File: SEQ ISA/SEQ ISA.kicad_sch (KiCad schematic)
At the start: 32 parts, among them IC1 TLX9310_TPL,F, J1 Conn_01x04_Pin, J2 Conn_01x01_Pin, J3 Conn_01x04_Pin, Q1 BS170F, SW1 PRISE JACK, SW2 SW_SPDT, U1 STM32L010C6T6R, U2 LD3985M33R_SOT23

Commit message: Seq review
added security button for launch detection, PWM motor and changd the regulator for a simpler one
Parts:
- removed C12: 100n, symbol Device:C
- removed U2: LD3985M33R_SOT23, Package_TO_SOT_SMD:SOT-23-5, symbol Regulator_Linear:LD3985M33R_SOT23
- added C7: 100n, symbol Device:C
- added M1: TOWERPRO SG90, symbol Motor:Motor_Servo
- added R6: 5.6k, symbol Device:R
- added SW3: INTERPTEUR, symbol Switch:SW_SPST
- added U3: LD1117S33TR_SOT223, Package_TO_SOT_SMD:SOT-223-3_TabPin2, symbol Regulator_Linear:LD1117S33TR_SOT223
- C13, C9: value 10n -> 100n
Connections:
- net GPIO_B5 is gone; now on net LAUNCH_STR: U1.41 (PB5)
- net +3.3V: now also SW3.1 (A), U3.2 (VO)
- net +5V: now also M1.2 (+)
- net GND: now also C7.2, M1.3 (-), U3.1 (GND)
- net VBAT: now also U3.3 (VI)
- net LAUNCH_STR: now reaches C9.1
- net LAUNCH_STR: now also C7.1, R6.2
- net GPIO_B4 renamed PWN_MOTOR
- net PWN_MOTOR: now also M1.1 (PWM)
- new net: R6.1, SW3.2 (B)
- no-connect marks 30 -> 28
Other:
- note added: "Boutton de sécurité"
- note added: "L'alimentation doit être différente de celle du séquenceur !"
- note added: "Ouverture de la trappe à parachute"
- note added: "Pensez à découpler le signale transmis: C:1Op"
- moved on the sheet: C13, C15, J3

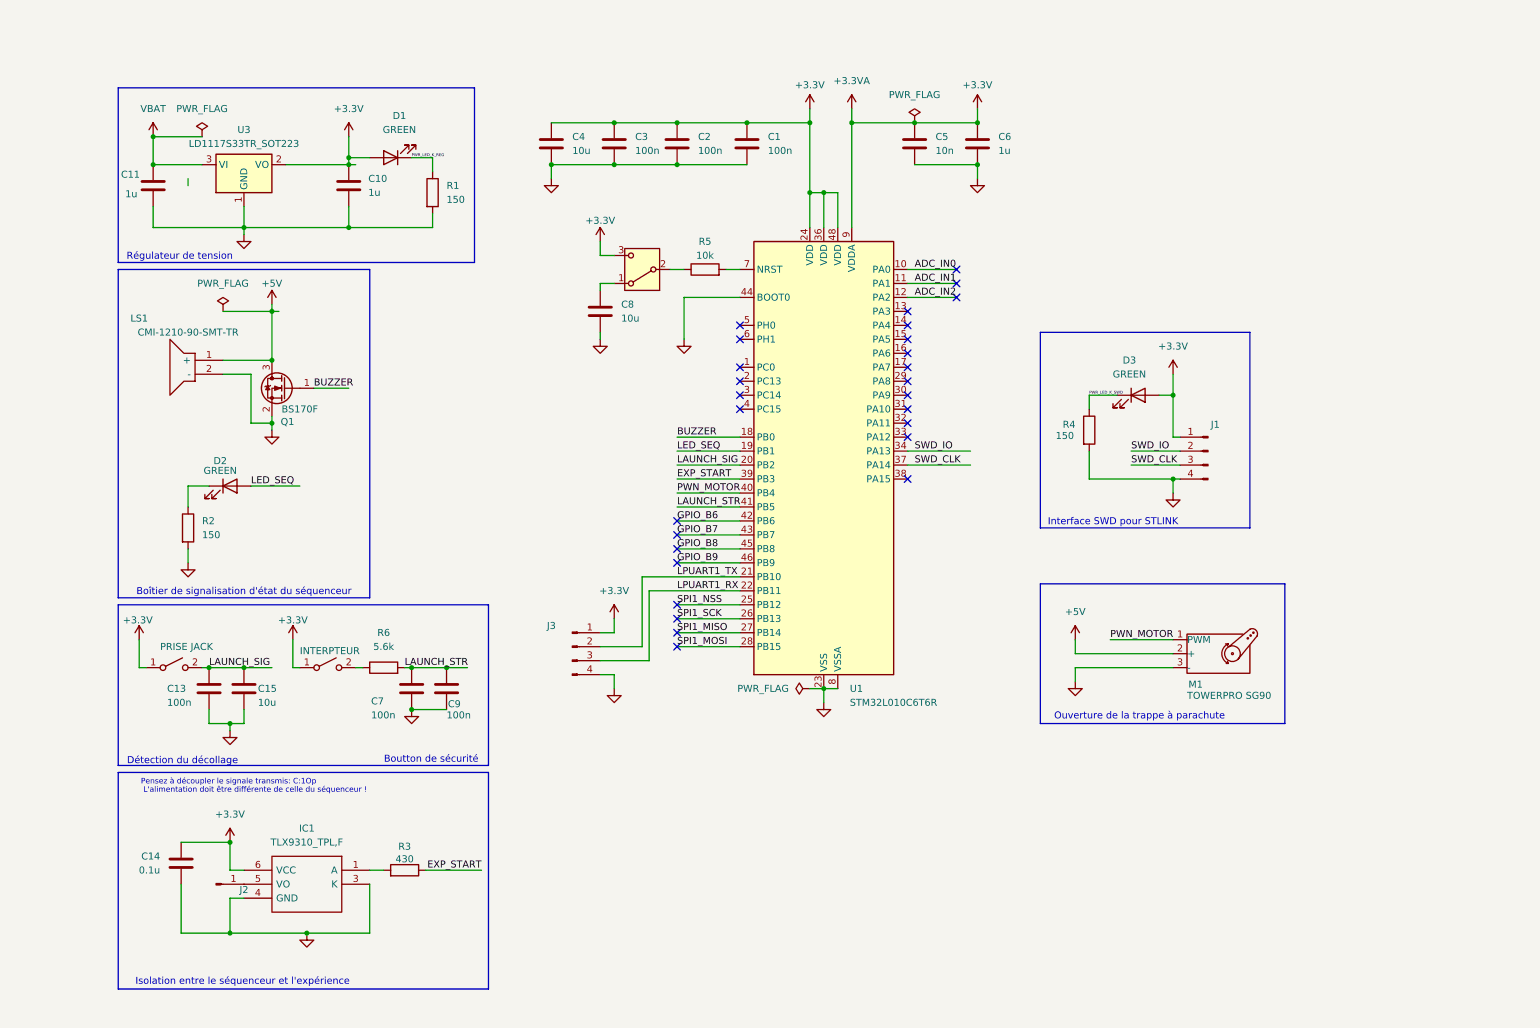
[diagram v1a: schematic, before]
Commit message: SEQ V2
Added servo motor controls, trigger button security for noise sensitive input and UART com
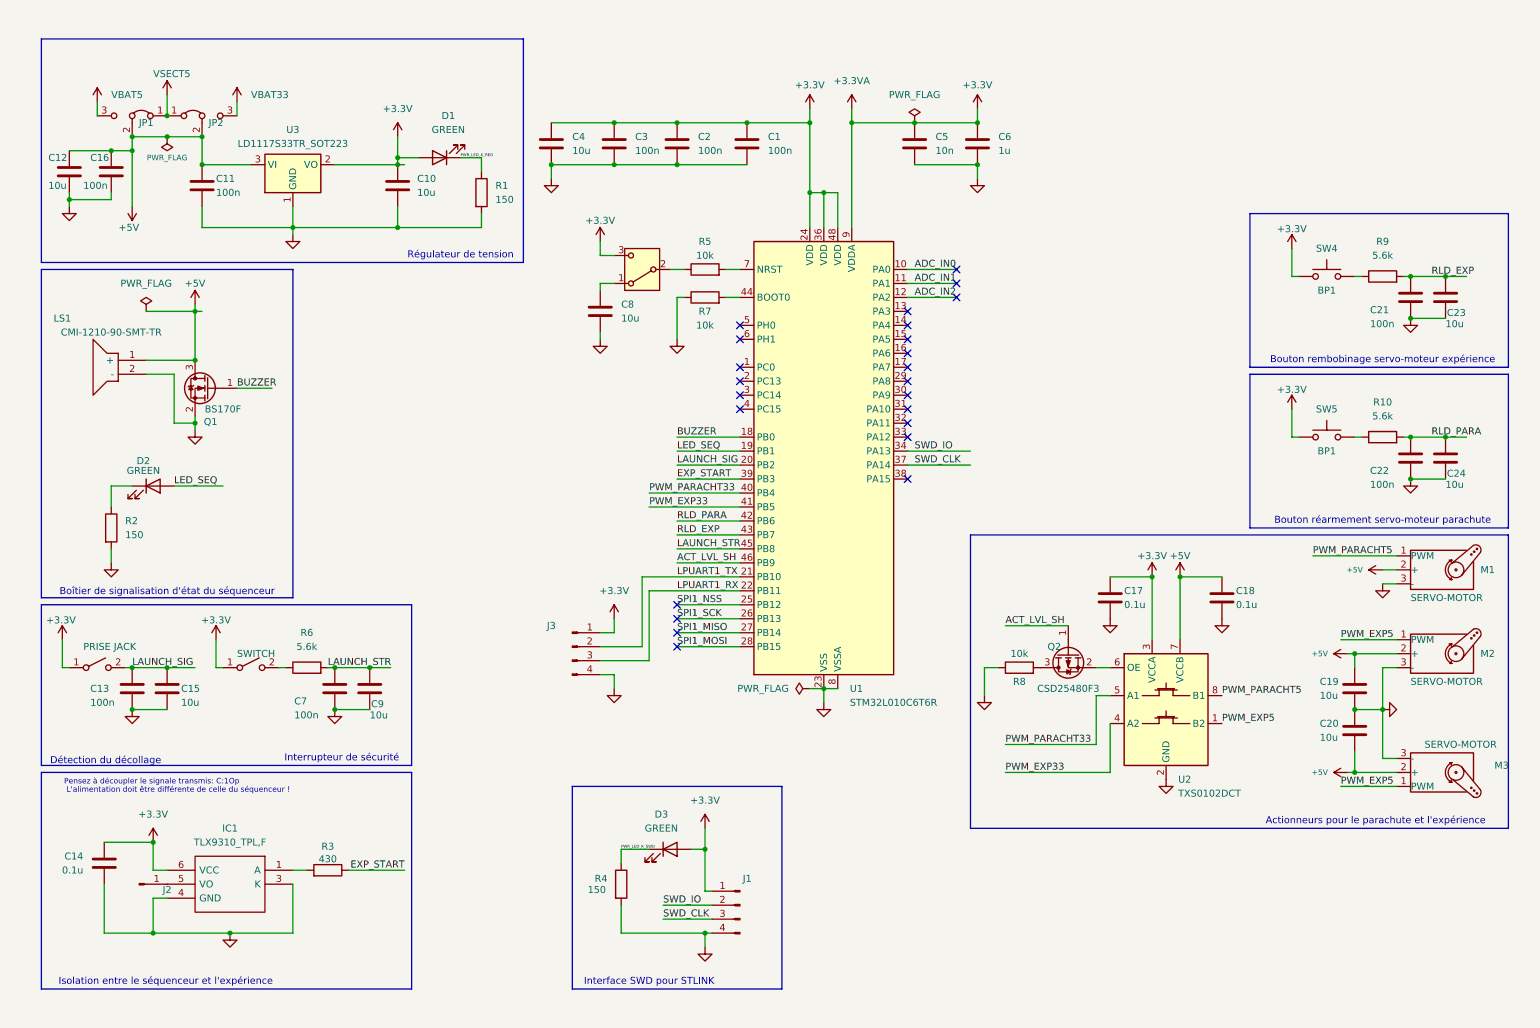
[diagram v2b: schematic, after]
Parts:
- added C12, C19, C20, C23, C24: 10u, symbol Device:C
- added C16, C21, C22: 100n, symbol Device:C
- added C17, C18: 0.1u, symbol Device:C
- added JP1, JP2: Jumper_3_Bridged12, symbol Jumper:Jumper_3_Bridged12
- added M2, M3: SERVO-MOTOR, symbol Motor:Motor_Servo
- added Q2: CSD25480F3, Package_DFN_QFN:Texas_PicoStar_DFN-3_0.69x0.60mm, symbol Transistor_FET:CSD25480F3
- added R10, R9: 5.6k, symbol Device:R
- added R7, R8: 10k, symbol Device:R
- added SW4, SW5: BP1, symbol Switch:SW_Push
- added U2: TXS0102DCT, Package_SO:SSOP-8_2.95x2.8mm_P0.65mm, symbol Logic_LevelTranslator:TXS0102DCT
- C10: value 1u -> 10u
- C11: value 1u -> 100n
- C9: value 100n -> 10u
- M1: value TOWERPRO SG90 -> SERVO-MOTOR
- SW3: value INTERPTEUR -> SWITCH
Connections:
- net GPIO_B8 is gone; now on net LAUNCH_STR: U1.45 (PB8)
- net VBAT is gone; now on net +5V: C11.1, U3.3 (VI)
- net +3.3V: now also C17.1, SW4.1, SW5.1, U2.3 (VCCA)
- net +5V: now also C12.1, C16.1, C18.1, C19.1, C20.2, JP1.2 (C), JP2.2 (C), M2.2 (+), M3.2 (+), U2.7 (VCCB)
- net GND: now also C12.2, C16.2, C17.2, C18.2, C19.2, C20.1, C21.2, C22.2, C23.2, C24.2, M2.3 (-), M3.3 (-), R7.1, R8.1, U2.2 (GND); no longer U1.44 (BOOT0)
- net LAUNCH_STR: no longer U1.41 (PB5)
- net GPIO_B6 renamed RLD_PARA
- net RLD_PARA: now also C22.1, C24.1, R10.2
- net GPIO_B7 renamed RLD_EXP
- net RLD_EXP: now also C21.1, C23.1, R9.2
- net GPIO_B9 renamed ACT_LVL_SH
- net ACT_LVL_SH: now also Q2.1 (G)
- net PWN_MOTOR renamed PWM_PARACHT33
- net PWM_PARACHT33: now also U2.5 (A1); no longer M1.1 (PWM)
- new net: R7.2, U1.44 (BOOT0)
- new net: Q2.3 (D), R8.2
- new net: R10.1, SW5.2
- new net: Q2.2 (S), U2.6 (OE)
- new net: R9.1, SW4.2
- new net PWM_EXP33: U1.41 (PB5), U2.4 (A2)
- new net PWM_EXP5: M2.1 (PWM), M3.1 (PWM), U2.1 (B2)
- new net PWM_PARACHT5: M1.1 (PWM), U2.8 (B1)
- new net VBAT33: JP2.3 (B)
- new net VBAT5: JP1.3 (B)
- new net VSECT5: JP1.1 (A), JP2.1 (A)
- no-connect marks 28 -> 24
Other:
- note added: "Actionneurs pour le parachute et l'expérience"
- note added: "Bouton rembobinage servo-moteur expérience"
- note added: "Bouton réarmement servo-moteur parachute"
- note added: "Interrupteur de sécurité"
- note removed: "Boutton de sécurité"
- note removed: "Ouverture de la trappe à parachute"
- moved on the sheet: C10, C11, C13, C14, C15, C7, C9, D1, D2, D3, IC1, J1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

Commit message: SEQ V2.1
Added test pads and protection resistance
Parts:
- removed Q2: CSD25480F3, Package_DFN_QFN:Texas_PicoStar_DFN-3_0.69x0.60mm, symbol Transistor_FET:CSD25480F3
- added JP3: Jumper_2_Bridged, symbol Jumper:Jumper_2_Bridged
- added R11: 5.6k, symbol Device:R
- added TP1, TP2, TP4, TP5: TestPoint, symbol Connector:TestPoint
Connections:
- net +3.3V: now also TP2.1, TP5.1
- net +5V: now also TP4.1
- net GND: now also TP1.1
- net LAUNCH_SIG: now also R11.2; no longer SW1.2 (B)
- net at R8.2: now also JP3.1 (A)
- net at U2.6 (OE): now also JP3.2 (B)
- new net: R11.1, SW1.2 (B)
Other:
- moved on the sheet: C13, C14, C15, C7, C9, R6

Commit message: Seq V3
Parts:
- removed C17, C18: 0.1u, symbol Device:C
- removed C19, C20: 10u, symbol Device:C
- removed D3: GREEN, symbol Device:LED
- removed J1, J3: Conn_01x04_Pin, symbol Connector:Conn_01x04_Pin
- removed JP3: Jumper_2_Bridged, symbol Jumper:Jumper_2_Bridged
- removed M1, M2, M3: SERVO-MOTOR, symbol Motor:Motor_Servo
- removed R8: 10k, symbol Device:R
- removed SW3: SWITCH, symbol Switch:SW_SPST
- removed TP2, TP4, TP5: TestPoint, symbol Connector:TestPoint
- removed U2: TXS0102DCT, Package_SO:SSOP-8_2.95x2.8mm_P0.65mm, symbol Logic_LevelTranslator:TXS0102DCT
- added IC2: SN74LVC4245ADW, ISA LIB:SN74LVC4345ADW, symbol SN74LVC4245ADW:SN74LVC4245ADW
- added J1: FTSH-107-01-L-DV-K-A, ISA LIB:FTSH-107-XX-YYY-DV-K-A, symbol FTSH-107-01-L-DV-K-A:FTSH-107-01-L-DV-K-A
- added M4, M5, M6: SERVO-MOTOR, Connector_PinHeader_2.54mm:PinHeader_1x03_P2.54mm_Vertical, symbol Motor:Motor_Servo
- added TP3, TP6: TestPoint, TestPoint:TestPoint_Pad_D3.0mm, symbol Connector:TestPoint
- C1, C10, C11, C12, C13, C14, C15, C16, C2, C21, C22, C23, C24, C3, C4, C5, C6, C8: footprint (none) -> Capacitor_SMD:C_0805_2012Metric
- C7: value 100n -> 0.1u; footprint (none) -> Capacitor_SMD:C_0805_2012Metric
- C9: value 10u -> 0.1u; footprint (none) -> Capacitor_SMD:C_0805_2012Metric
- D1, D2: footprint (none) -> LED_SMD:LED_0805_2012Metric
- IC1: footprint TLP2355E -> ISA LIB:TLX9310
- J2: footprint (none) -> Connector_JST:JST_XH_B1B-XH-AM_1x01_P2.50mm_Vertical
- JP1, JP2: footprint (none) -> Jumper:SolderJumper-3_P1.3mm_Open_Pad1.0x1.5mm_NumberLabels
- LS1: footprint CMI121090SMTTR -> ISA LIB:CMI121090SMTTR
- R1, R10, R11, R2, R3, R5, R7, R9: footprint (none) -> Resistor_SMD:R_0805_2012Metric
- R4: value 150 -> 10k; footprint (none) -> Resistor_SMD:R_0805_2012Metric
- R6: value 5.6k -> 10k; footprint (none) -> Resistor_SMD:R_0805_2012Metric
- TP1: footprint (none) -> TestPoint:TestPoint_Pad_D3.0mm
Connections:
- net PWR_LED_K_SWD is gone; now on net GND: R4.1
- net +3.3V: now also C7.1, IC2.23 (VCCB_(3.3_V)_1), IC2.24 (VCCB_(3.3_V)_2), J1.3; no longer C14.1, IC1.6 (VCC)
- net +5V: now also C9.1, R6.2, IC2.1 ((5_V)_VCCA), M4.2 (+), M5.2 (+), M6.2 (+); no longer Q1.3 (D)
- net GND: now also IC2.10 (A8), IC2.11 (GND_1), IC2.12 (GND_2), IC2.13 (GND_3), IC2.14 (B8), IC2.15 (B7), IC2.9 (A7), J1.11, J1.5, J1.7, M4.3 (-), M5.3 (-), M6.3 (-); no longer LS1.2 (-), R4.2
- net LPUART1_RX: now also J1.13
- net LPUART1_TX: now also J1.14
- net PWM_PARACHT5: now also IC2.20 (B2), IC2.21 (B1), IC2.3 (A1), IC2.4 (A2), M6.1 (PWM)
- net RLD_EXP: now also U1.45 (PB8); no longer U1.43 (PB7)
- net RLD_PARA: now also U1.43 (PB7); no longer U1.42 (PB6)
- net SWD_CLK: now also J1.6
- net SWD_IO: now also J1.4
- net at R6.1: now also IC2.22 (~{OE})
- net NRST: now reaches R5.2, U1.7 (NRST)
- net NRST: now also J1.12
- net ACT_LVL_SH: no longer names the net of U1.46 (PB9)
- removed net LAUNCH_STR: C7.1, C9.1, R6.2, U1.45 (PB8)
- net PWM_EXP33 renamed PWM1_EXP33
- net PWM1_EXP33: now also IC2.18 (B4), IC2.19 (B3)
- net VBAT33 renamed VBATMIC
- net VBATMIC: now also TP6.1
- net VBAT5 renamed VBATACT
- net VBATACT: now also TP3.1
- new net: LS1.2 (-), Q1.3 (D)
- new net: IC2.2 (DIR), R4.2
- new net +3.3VEXP: C14.1, IC1.6 (VCC)
- new net PWM1_EXP5: IC2.5 (A3), IC2.6 (A4), M4.1 (PWM)
- new net PWM2_EXP33: IC2.16 (B6), IC2.17 (B5), U1.42 (PB6)
- new net PWM2_EXP5: IC2.7 (A5), IC2.8 (A6), M5.1 (PWM)
- no-connect marks 24 -> 30
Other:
- note added: "Interface SWD pour STLINK-V3SET"
- note removed: "Interface SWD pour STLINK"
- note removed: "Interrupteur de sécurité"
- moved on the sheet: C21, C22, C23, C24, Q1, R10, R5, R9, SW4, SW5

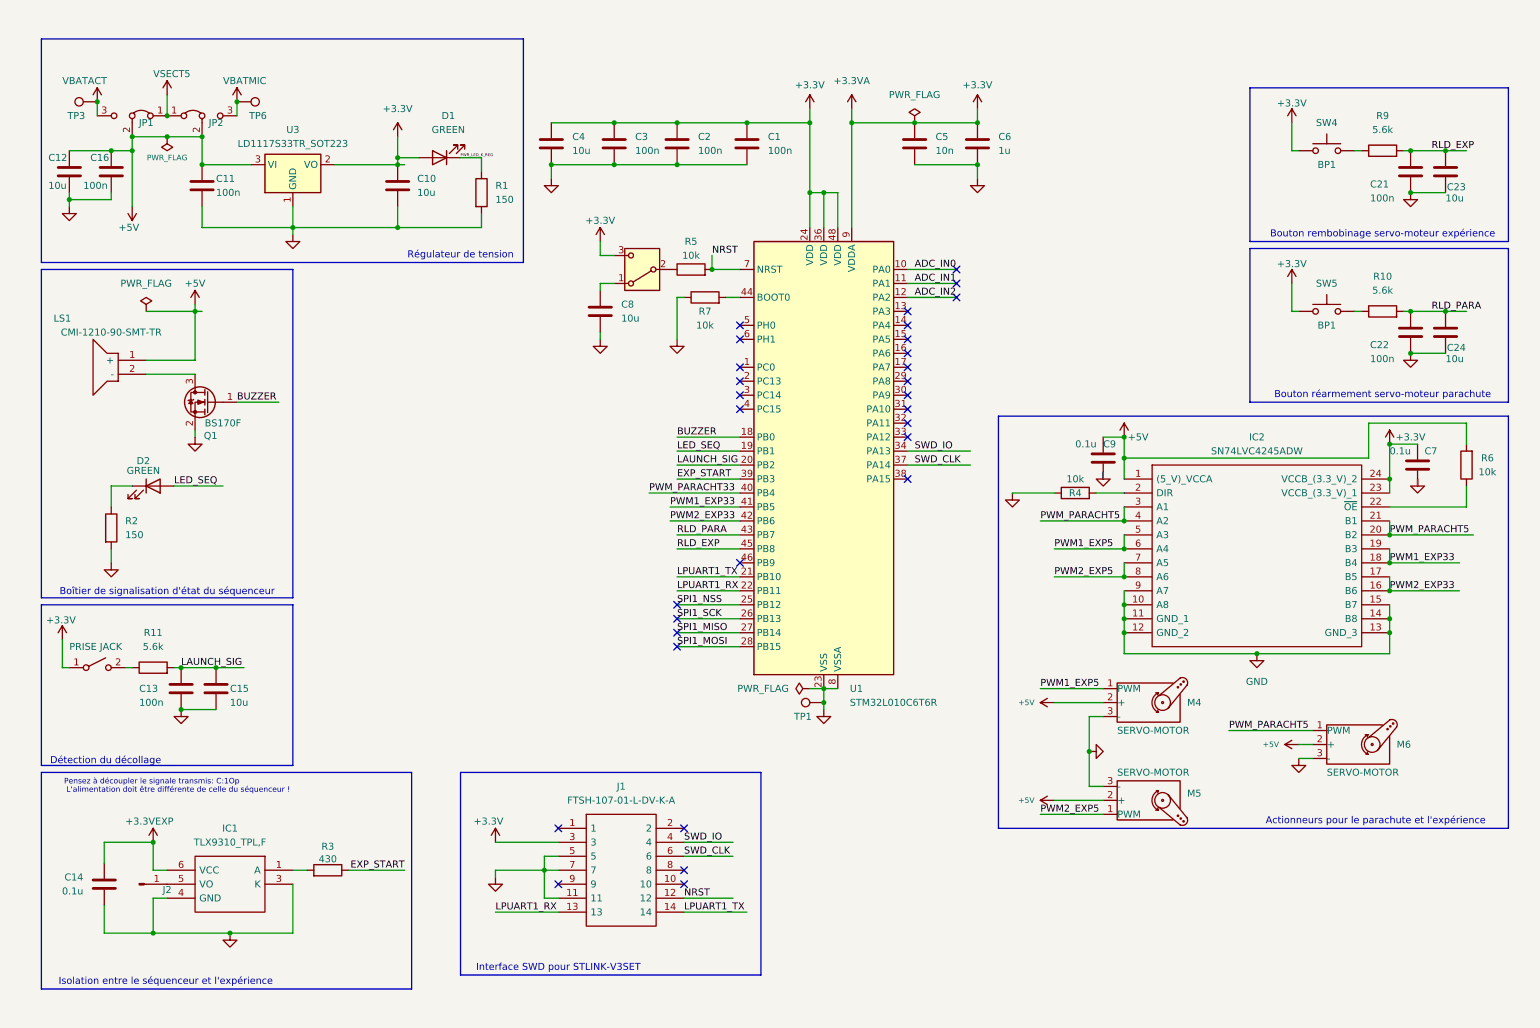
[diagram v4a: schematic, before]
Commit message: Started Fottprinting
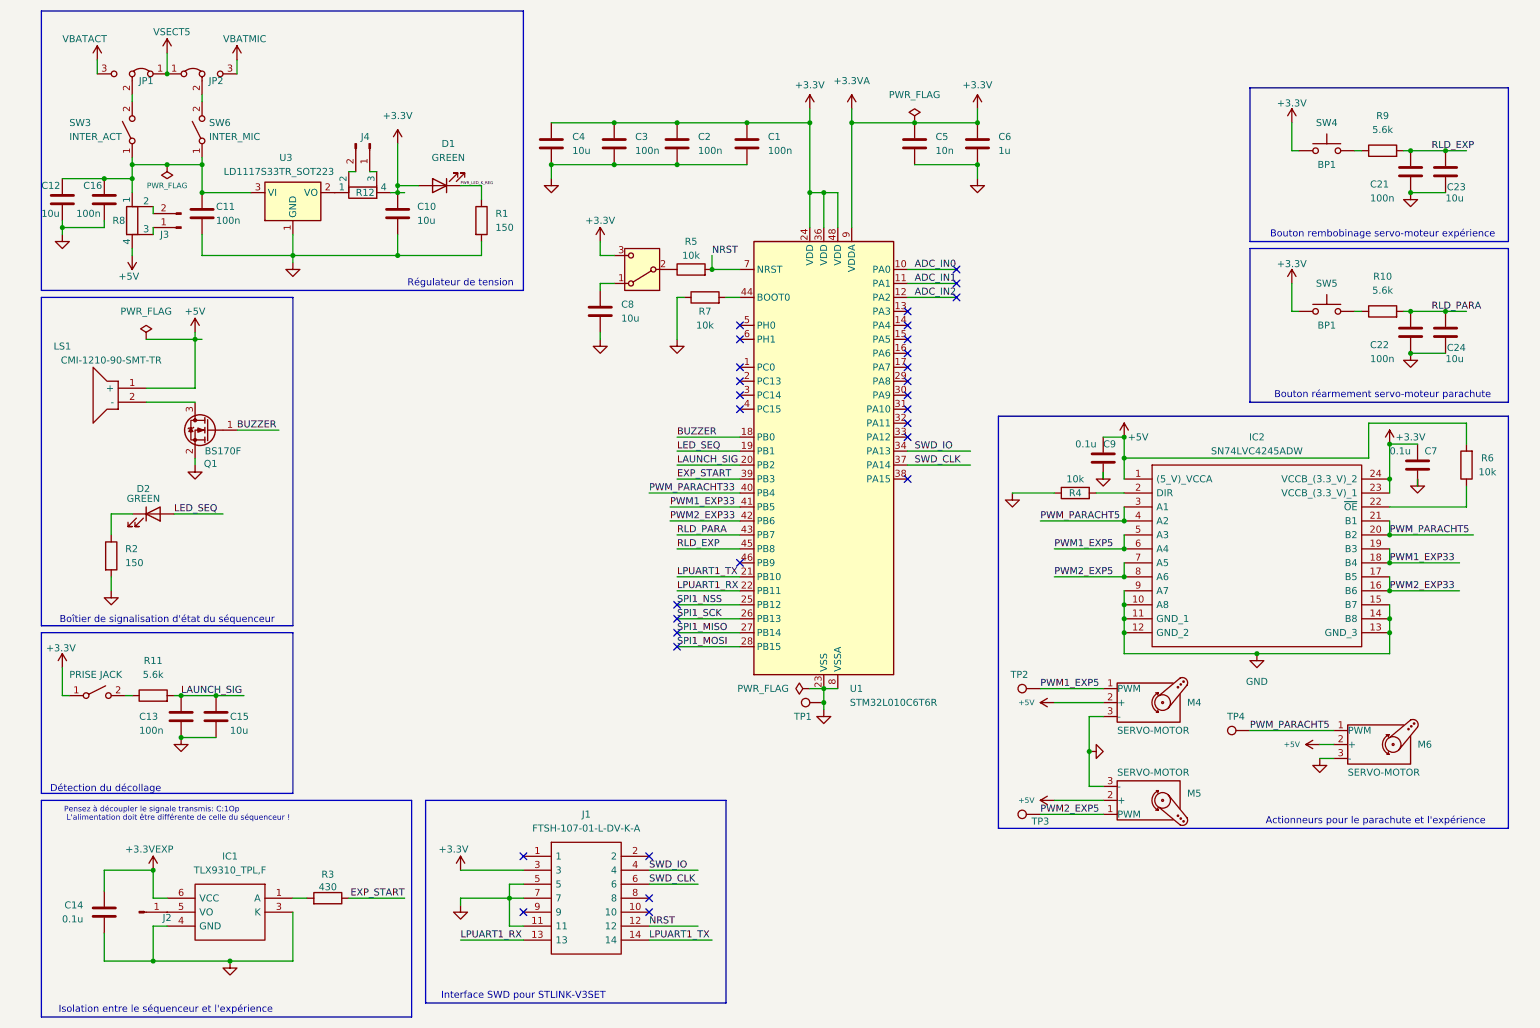
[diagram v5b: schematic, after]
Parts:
- removed TP6: TestPoint, TestPoint:TestPoint_Pad_D3.0mm, symbol Connector:TestPoint
- added J3, J4: Conn_01x02_Pin, Connector_PinHeader_2.54mm:PinHeader_1x02_P2.54mm_Vertical, symbol Connector:Conn_01x02_Pin
- added R12, R8: R_Shunt, Resistor_SMD:R_Shunt_Ohmite_LVK12, symbol Device:R_Shunt
- added SW3: INTER_ACT, symbol Switch:SW_SPST
- added SW6: INTER_MIC, symbol Switch:SW_SPST
- added TP2, TP4: TestPoint, TestPoint:TestPoint_Pad_D3.0mm, symbol Connector:TestPoint
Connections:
- net +3.3V: now also R12.4; no longer U3.2 (VO)
- net +5V: now also R8.4; no longer C11.1, C12.1, C16.1, JP1.2 (C), JP2.2 (C), U3.3 (VI)
- net PWM1_EXP5: now also TP2.1
- net PWM2_EXP5: now also TP3.1
- net PWM_PARACHT5: now also TP4.1
- net VBATACT: no longer TP3.1
- new net: J3.1 (Pin_1), R8.3
- new net: J3.2 (Pin_2), R8.2
- new net: JP1.2 (C), SW3.2 (B)
- new net: J4.1 (Pin_1), R12.3
- new net: J4.2 (Pin_2), R12.2
- new net: C11.1, C12.1, C16.1, R8.1, SW3.1 (A), SW6.1 (A), U3.3 (VI)
- new net: JP2.2 (C), SW6.2 (B)
- new net: R12.1, U3.2 (VO)
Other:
- moved on the sheet: C10, C11, C12, C13, C14, C15, C16, D1, D2, IC1, J1, J2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
